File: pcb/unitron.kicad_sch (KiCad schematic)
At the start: 67 parts, among them J1 Conn_01x10_Male, J2 Conn_01x10_Female, J3 Conn_01x10_Male, J4 Conn_01x10_Female, Q1 FDN340P, Q2 BSS123, SW1 SW_SPST, U1 LTC-4727JS, U2 LTC-4727JS, U3 AS1115-BSST, U4 QT_Py, U5 MCP73831-2-OT, U6 LTC-4727JR, U7 LTC-4727JR, U8 AS1115-BSST

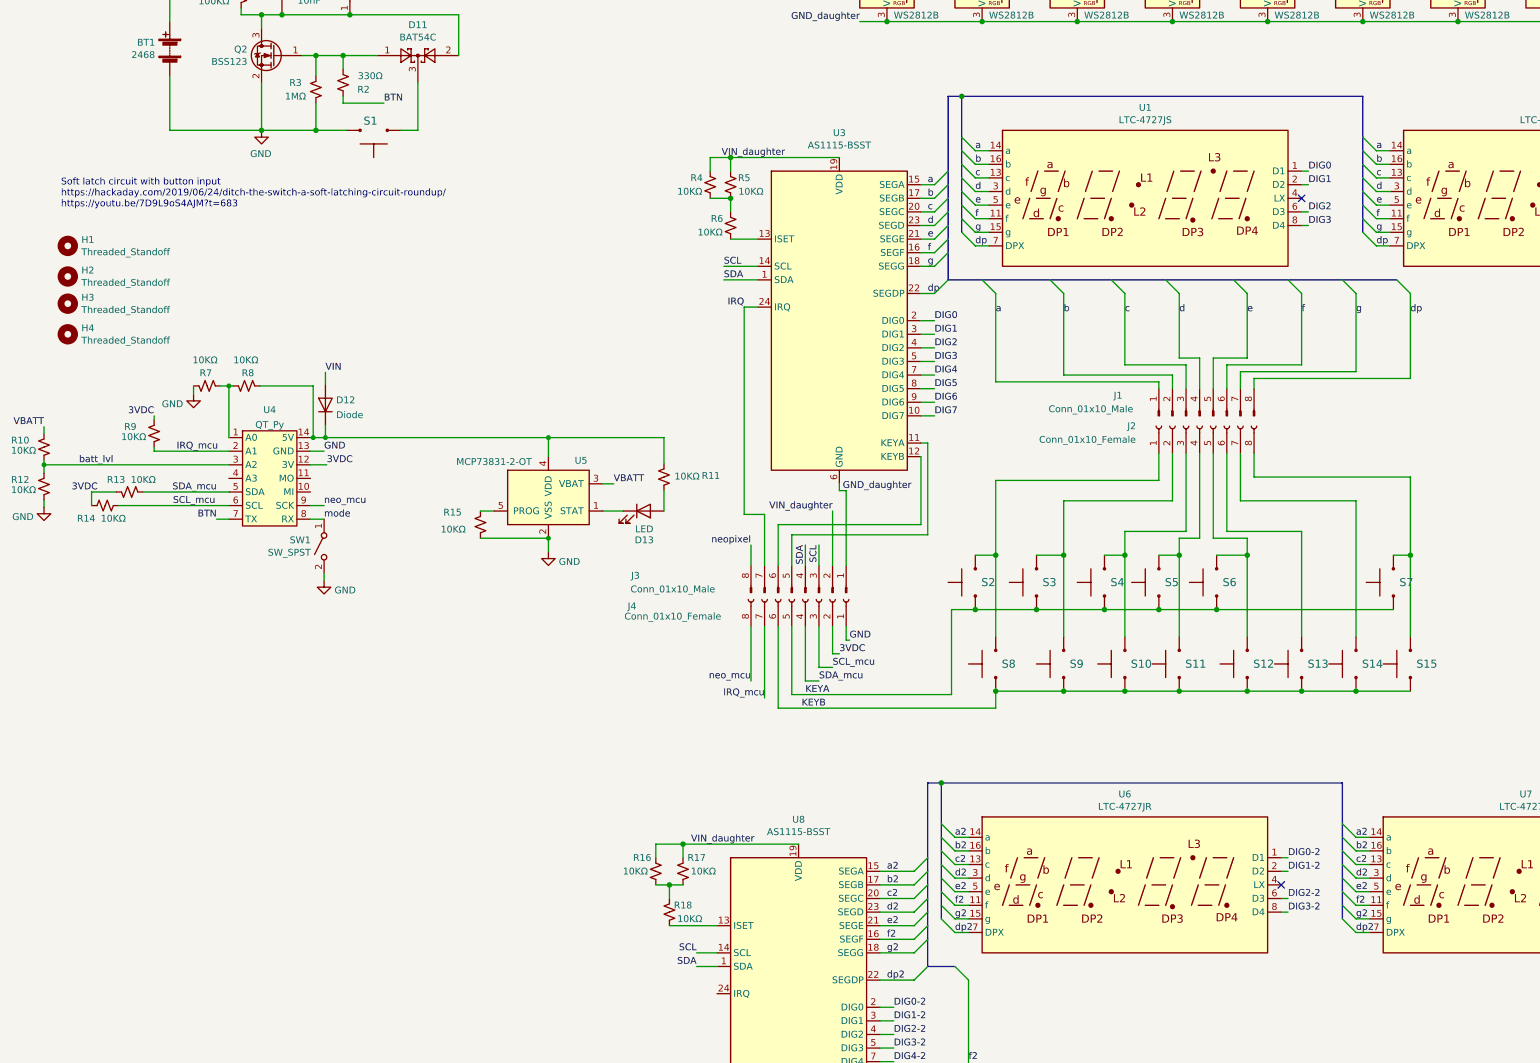
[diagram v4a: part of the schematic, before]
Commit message: v1.10
shift as1115 label closer to pin 1
remove "1"  label from km neopixel
make IRQ trace and via larger.
change i2c pullups from 10k to 2k
added diodes to keyscan traces so multiple buttons can simultaneously be pressed
make cutout for different qt py
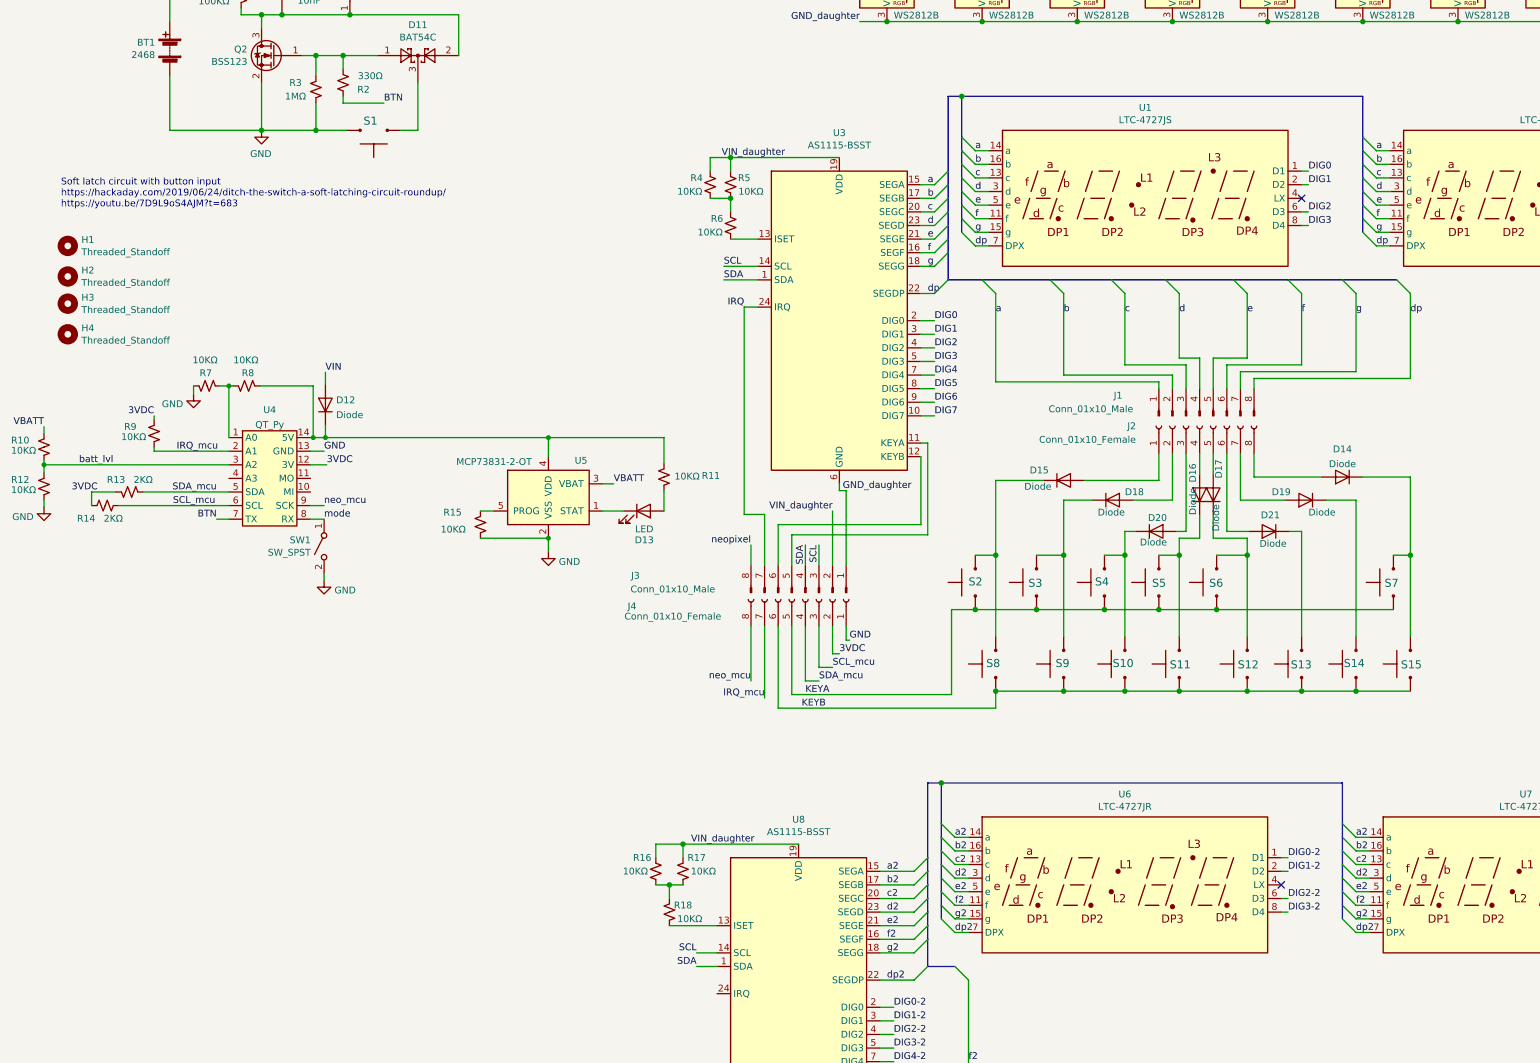
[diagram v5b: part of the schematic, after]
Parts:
- added D14, D15, D16, D17, D18, D19, D20, D21: Diode, asl_footprints:D_SOD-123F, symbol asl_symbols_new:Diode
- R13, R14: value 10KΩ -> 2KΩ
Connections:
- net at S2.2, S8.2: now also D15.1 (K); no longer J2.1 (Pin_1)
- net at S3.2, S9.2: now also D18.1 (K); no longer J2.2 (Pin_2)
- net at S10.2, S4.2: now also D20.1 (K); no longer J2.3 (Pin_3)
- net at S11.2, S5.2: now also D16.1 (K); no longer J2.4 (Pin_4)
- net at S13.2: now also D21.1 (K); no longer J2.6 (Pin_6)
- net at S12.2, S6.2: now also D17.1 (K); no longer J2.5 (Pin_5)
- net at S15.2, S7.2: now also D14.1 (K); no longer J2.8 (Pin_8)
- net at S14.2: now also D19.1 (K); no longer J2.7 (Pin_7)
- new net: D19.2 (A), J2.7 (Pin_7)
- new net: D20.2 (A), J2.3 (Pin_3)
- new net: D21.2 (A), J2.6 (Pin_6)
- new net: D16.2 (A), J2.4 (Pin_4)
- new net: D15.2 (A), J2.1 (Pin_1)
- new net: D18.2 (A), J2.2 (Pin_2)
- new net: D17.2 (A), J2.5 (Pin_5)
- new net: D14.2 (A), J2.8 (Pin_8)

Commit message: v 1.11
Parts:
- removed C1: 10nF, Capacitor_SMD:C_0805_2012Metric, symbol Device:C
- removed D11: BAT54C, Package_TO_SOT_SMD:SOT-23, symbol Diode:BAT54C
- removed Q1: FDN340P, Package_TO_SOT_SMD:SOT-23, symbol asl_symbols:FDN340P
- removed Q2: BSS123, Package_TO_SOT_SMD:SOT-23, symbol Transistor_FET:BSS123
- added C2, C3: 10nF, Capacitor_SMD:C_0805_2012Metric, symbol Device:C
- added R19, R20, R21, R22, R23, R24, R25: 10KΩ, Resistor_SMD:R_0805_2012Metric, symbol Device:R_Small_US
- added TP1, TP2, TP3: TestPoint, TestPoint:TestPoint_Pad_1.0x1.0mm, symbol Connector:TestPoint
- R1: value 100KΩ -> 10Ω
- R13, R14: value 2KΩ -> 1KΩ
- R2: value 330Ω -> 10Ω
- R3: value 1MΩ -> 10KΩ
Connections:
- net VIN is gone; now on net VBATT: D12.2 (A)
- net BTN: now also S1.1; no longer R2.1
- net GND: no longer R3.1
- net GND_daughter: now also C2.1, C3.2
- net IRQ: now also TP3.1
- net SCL: now also R2.2, TP1.1; no longer J3.3 (Pin_3)
- net SDA: now also R1.2, TP2.1; no longer J3.4 (Pin_4)
- net VBATT: no longer R1.2
- net VIN_daughter: now also C2.2, C3.1
- net a: now also R3.2; no longer J1.1 (Pin_1)
- net b: now also R19.2; no longer J1.2 (Pin_2)
- net c: now also R21.2; no longer J1.3 (Pin_3)
- net d: now also R20.2; no longer J1.4 (Pin_4)
- net dp: now also R25.2; no longer J1.8 (Pin_8)
- net e: now also R22.2; no longer J1.5 (Pin_5)
- net f: now also R23.2; no longer J1.6 (Pin_6)
- net g: now also R24.2; no longer J1.7 (Pin_7)
- net at R1.1: now also J3.4 (Pin_4)
- new net: J3.3 (Pin_3), R2.1
- new net: J1.3 (Pin_3), R21.1
- new net: J1.8 (Pin_8), R25.1
- new net: J1.2 (Pin_2), R19.1
- new net: J1.1 (Pin_1), R3.1
- new net: J1.6 (Pin_6), R23.1
- new net: J1.5 (Pin_5), R22.1
- new net: J1.4 (Pin_4), R20.1
- new net: J1.7 (Pin_7), R24.1
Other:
- note removed: "Soft latch circuit with button input https://hackaday.com/2019/06/24/ditch-the-switch-a-soft-latching-circuit-roundup/ https://youtu.be/7D9L9oS4AJM?t=683"
- moved on the sheet: BT1, D13, H1, H2, H3, H4, J3, J4, R11, R15, S1, U5

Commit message: pcb v1.12
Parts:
- removed D14, D15, D16, D17, D18, D19, D20, D21: Diode, asl_footprints:D_SOD-123F, symbol asl_symbols_new:Diode
- removed R1, R2: 10Ω, Resistor_SMD:R_0805_2012Metric, symbol Device:R_Small_US
- added SW1: SPST_B12AP, asl_footprints:switch_toggle, symbol asl_symbols:SPST_B12AP
- C1: renamed from C2; value 10nF -> 1µF
- C2: renamed from C3; value 10nF -> 100nF
- R18: renamed from R13; value 1KΩ -> 2KΩ
- R19: renamed from R14; value 1KΩ -> 2KΩ
- R20: renamed from R15; value 10KΩ -> 2KΩ
- renumbered D12 to D11, D13 to D12, R4 to R1, R24 to R10, R25 to R11, R7 to R12, R8 to R13, R9 to R14, R10 to R15, R11 to R16, R12 to R17, R5 to R2, R16 to R21, R17 to R22, R18 to R23, R6 to R3, R3 to R4, R19 to R5, R20 to R6, R21 to R7, R22 to R8, R23 to R9, SW1 to SW2
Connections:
- net SCL: now also J3.3 (Pin_3)
- net SDA: now also J3.4 (Pin_4)
- net VBATT: now also SW1.2 (B); no longer BT1.1 (+)
- net at S2.2, S8.2: now also J2.1 (Pin_1)
- net at S3.2, S9.2: now also J2.2 (Pin_2)
- net at S10.2, S4.2: now also J2.3 (Pin_3)
- net at S11.2, S5.2: now also J2.4 (Pin_4)
- net at S13.2: now also J2.6 (Pin_6)
- net at S12.2, S6.2: now also J2.5 (Pin_5)
- net at S15.2, S7.2: now also J2.8 (Pin_8)
- net at S14.2: now also J2.7 (Pin_7)
- new net: BT1.1 (+), SW1.1 (A)

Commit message: pcb v1.13
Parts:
- removed D10, D7, D8, D9: WS2812B, LED_SMD:LED_WS2812B_PLCC4_5.0x5.0mm_P3.2mm, symbol LED:WS2812B
- removed S6: Gateron Blue, Button_Switch_Keyboard:SW_Cherry_MX_1.00u_PCB, symbol imperializer-rescue:switch_momentary_2pin-asl_symbols-imperializer-rescue
- removed SW1: SPST_B12AP, asl_footprints:switch_toggle, symbol asl_symbols:SPST_B12AP
- removed U5: MCP73831-2-OT, Package_TO_SOT_SMD:SOT-23-5, symbol Battery_Management:MCP73831-2-OT
- added C3: 10µF, Capacitor_SMD:C_0805_2012Metric, symbol Device:C
- added SW1: SPST, asl_footprints:switch_toggle, symbol asl_symbols_new:SPST_B12AP
- added SW3: RotaryEncoder_Switch, asl_footprints:encoder_PEC11R, symbol Device:RotaryEncoder_Switch
- added U5: MCP73831, Package_TO_SOT_SMD:SOT-23-5, symbol asl_symbols_new:MCP73831
- renumbered D11 to D7, D12 to D8, S11 to S10, S12 to S11, S13 to S12, S14 to S13, S15 to S14, S7 to S6, S8 to S7, S9 to S8, S10 to S9
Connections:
- net GND: now also C3.2, SW3.C, SW3.S2, U5.2 (VSS)
- net IRQ_mcu: no longer R14.2, U4.2 (A1)
- net VBATT: now also C3.1, SW1.2 (B), U5.3 (VBAT)
- net at BT1.1 (+): now also SW1.1 (A)
- net at R20.2: now also U5.5 (PROG)
- net at D7.1 (K), R13.1, R16.1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: now also U5.4 (VDD)
- net at D8.1 (K): now also U5.1 (STAT)
- net encoder_b: now reaches U4.10 (MI)
- net encoder_b: now also SW3.B
- net encoder_a: now reaches U4.11 (MO)
- net encoder_a: now also SW3.A
- net encoder_btn: now reaches U4.4 (A3)
- net encoder_btn: now also SW3.S1
- new net: R14.2, U4.2 (A1)
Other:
- moved on the sheet: BT1, D1, D2, D3, D4, D5, D6, D7, D8, R12, R13, R14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
